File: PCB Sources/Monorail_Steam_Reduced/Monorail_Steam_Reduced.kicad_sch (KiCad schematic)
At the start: 140 parts, among them J6 USB_C_Receptacle_USB2.0, J8 Conn_01x04_Male, J9 Conn_01x03_Male, SW3 RotaryEncoder_Switch, U1 SRV05-4, U2 XC6206PxxxMR, U3 RP2040TR7, U4 W25Q128JVS, Y1 Crystal_GND24_Small

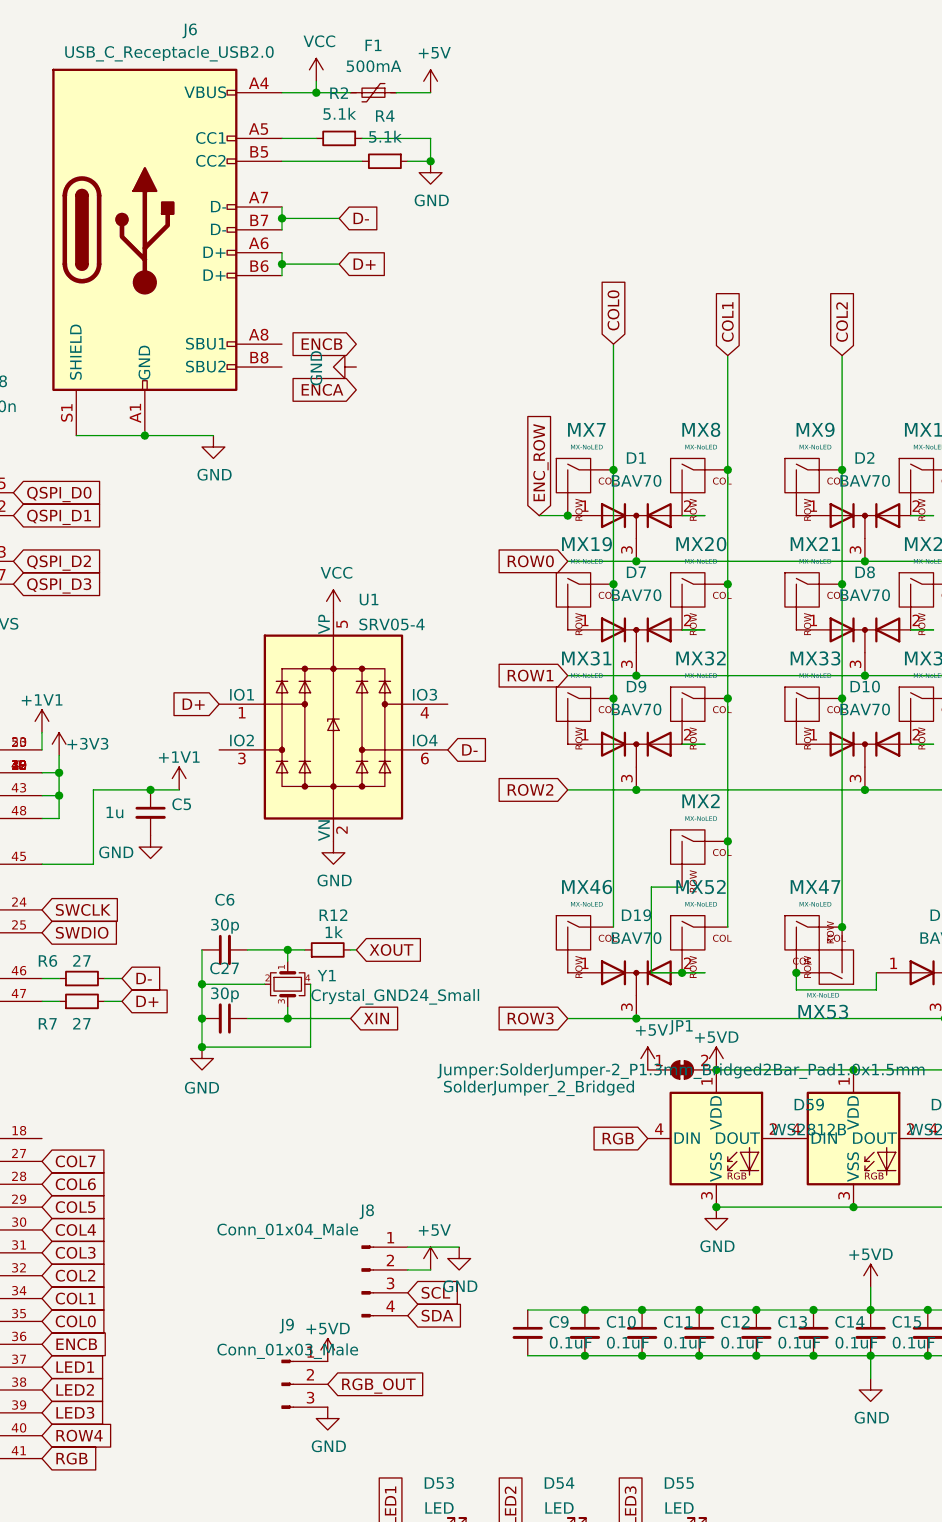
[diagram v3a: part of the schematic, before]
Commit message: set initial positions for components
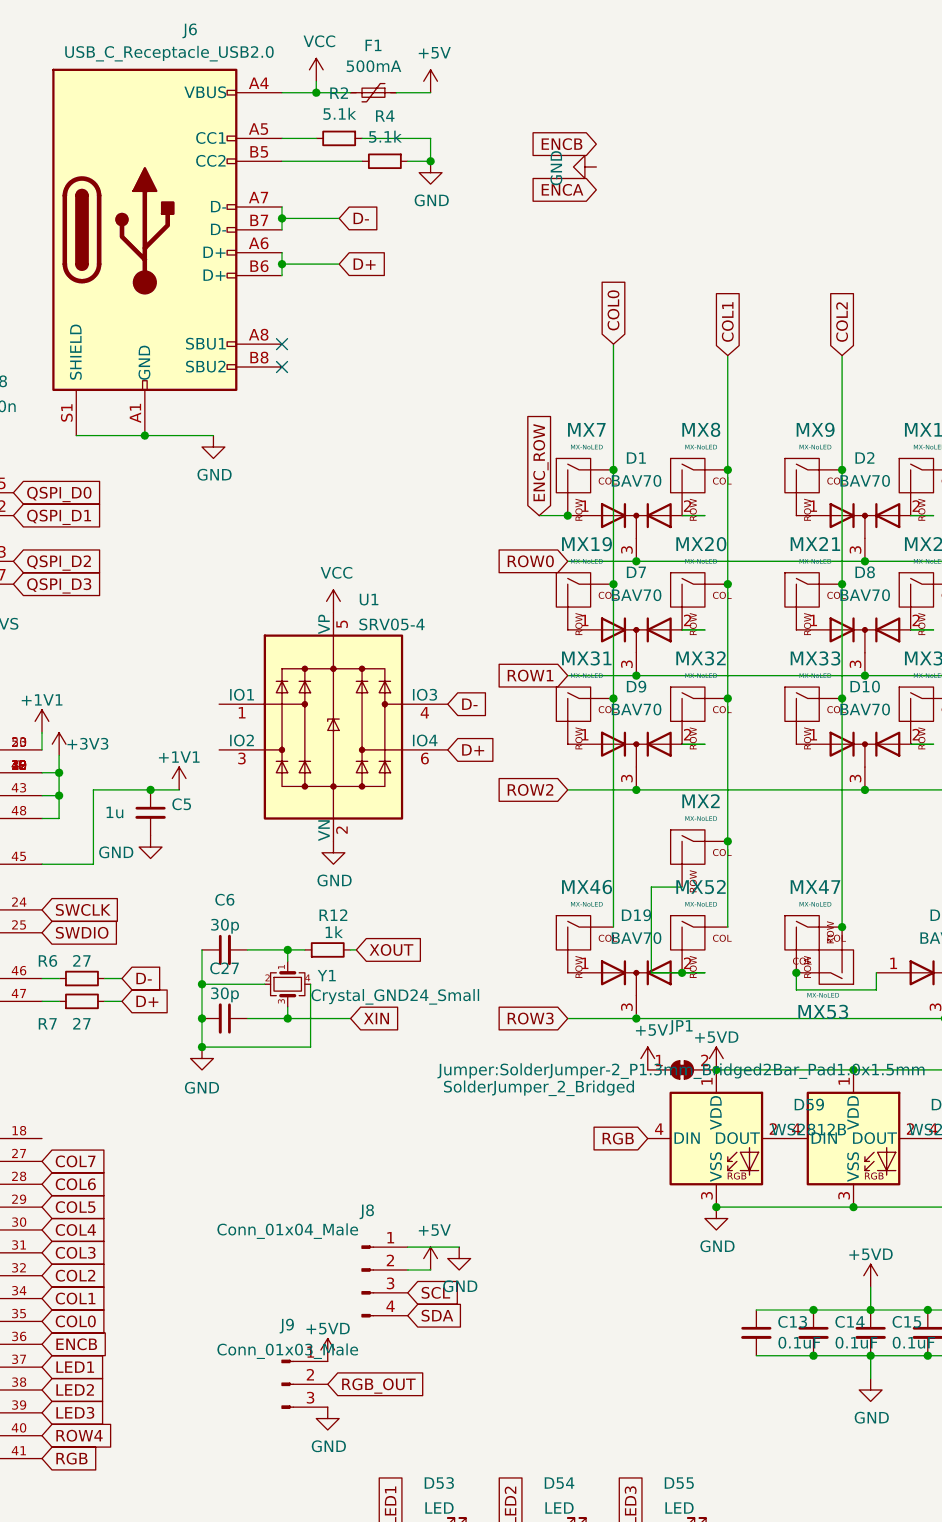
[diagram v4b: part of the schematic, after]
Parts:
- removed C10, C11, C12, C9: 0.1uF, Capacitor_SMD:C_0603_1608Metric, symbol Device:C_Small
- J6: footprint Type-C:HRO-TYPE-C-31-M-12-Assembly -> Connector_USB:USB_C_Receptacle_HRO_TYPE-C-31-M-12
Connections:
- net D+: now also U1.6 (IO4); no longer U1.1 (IO1)
- net D-: now also U1.4 (IO3); no longer U1.6 (IO4)
- no-connect marks 0 -> 2

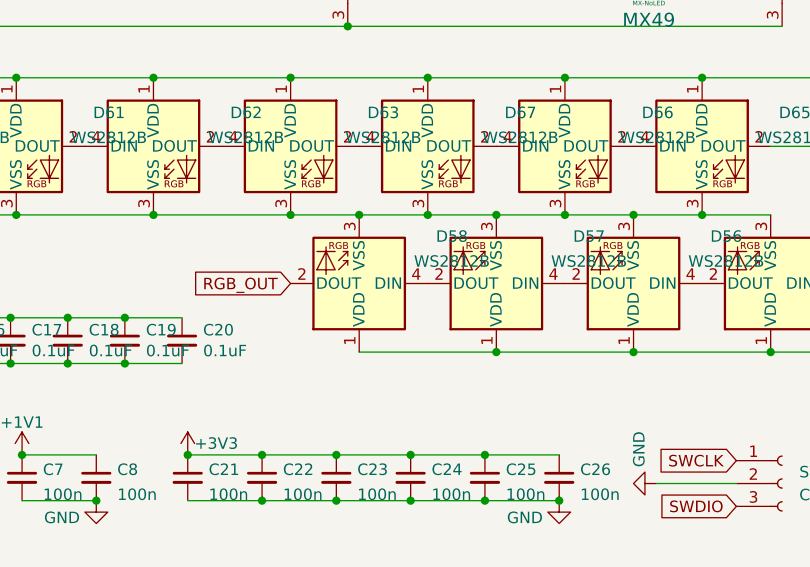
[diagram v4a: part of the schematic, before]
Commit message: began routing upper portion, improved placement
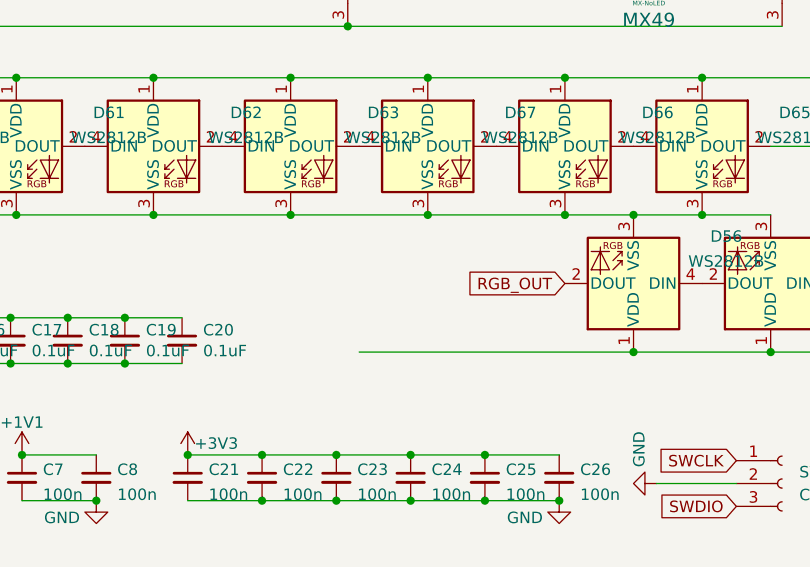
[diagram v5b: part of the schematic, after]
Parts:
- removed D57, D58: WS2812B, WS2812B:WS2812B_data-bridgeable, symbol LED:WS2812B
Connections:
- net RGB_OUT: now also D56.2 (DOUT)
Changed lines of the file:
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@@
   (junction (at 60.325 52.07) (diameter 0) (color 0 0 0 0)
   )
-  (junction (at 219.71 145.415) (diameter 0) (color 0 0 0 0)
-  )
   (junction (at 190.5 88.9) (diameter 0) (color 0 0 0 0)
   )
@@
   (junction (at 193.675 161.925) (diameter 0) (color 0 0 0 0)
   )
-  (junction (at 234.95 145.415) (diameter 0) (color 0 0 0 0)
-  )
   (junction (at 225.425 177.165) (diameter 0) (color 0 0 0 0)
   )
@@
   (junction (at 241.935 177.165) (diameter 0) (color 0 0 0 0)
   )
-  (junction (at 234.95 160.655) (diameter 0) (color 0 0 0 0)
-  )
   (junction (at 265.43 160.655) (diameter 0) (color 0 0 0 0)
   )
@@
     (stroke (width 0) (type default))
   )
-  (wire (pts (xy 219.71 145.415) (xy 227.33 145.415))
+  (wire (pts (xy 212.09 145.415) (xy 227.33 145.415))
     (stroke (width 0) (type default))
   )
@@
     (stroke (width 0) (type default))
   )
-  (wire (pts (xy 234.95 145.415) (xy 242.57 145.415))
+  (wire (pts (xy 227.33 145.415) (xy 242.57 145.415))
     (stroke (width 0) (type default))
   )
@@
     (stroke (width 0) (type default))
   )
-  (wire (pts (xy 219.71 160.655) (xy 234.95 160.655))
+  (wire (pts (xy 219.71 160.655) (xy 250.19 160.655))
     (stroke (width 0) (type default))
   )
@@
     (stroke (width 0) (type default))
   )
-  (wire (pts (xy 212.09 145.415) (xy 219.71 145.415))
-    (stroke (width 0) (type default))
-  )
   (wire (pts (xy 210.82 106.68) (xy 210.82 119.38))
     (stroke (width 0) (type default))
@@
     (stroke (width 0) (type default))
   )
-  (wire (pts (xy 227.33 145.415) (xy 234.95 145.415))
-    (stroke (width 0) (type default))
-  )
   (wire (pts (xy 259.08 119.38) (xy 261.62 119.38))
     (stroke (width 0) (type default))
@@
     (stroke (width 0) (type default))
   )
-  (wire (pts (xy 234.95 160.655) (xy 250.19 160.655))
-    (stroke (width 0) (type default))
-  )
   (wire (pts (xy 203.2 50.8) (xy 203.2 63.5))
     (stroke (width 0) (type default))
@@
     )
   )
-  (global_label "RGB_OUT" (shape input) (at 212.09 153.035 180) (fields_autoplaced)
+  (global_label "RGB_OUT" (shape input) (at 242.57 153.035 180) (fields_autoplaced)
     (effects (font (size 1.27 1.27)) (justify right))
-    (property "Intersheetrefs" "${INTERSHEET_REFS}" (at 201.3596 152.9556 0)
+    (property "Intersheetrefs" "${INTERSHEET_REFS}" (at 231.8396 152.9556 0)
       (effects (font (size 1.27 1.27)) (justify right) hide)
     )
@@
     )
   )
-  (symbol (lib_id "LED:WS2812B") (at 219.71 153.035 180) (unit 1)
-    (in_bom yes) (on_board yes) (dnp no) (fields_autoplaced)
-    (property "Reference" "D58" (at 230.0159 147.811 0)
-      (effects (font (size 1.27 1.27)))
-    )
-    (property "Value" "WS2812B" (at 230.0159 150.5861 0)
-      (effects (font (size 1.27 1.27)))
-    )
-    (property "Footprint" "WS2812B:WS2812B_data-bridgeable" (at 218.44 145.415 0)
-      (effects (font (size 1.27 1.27)) (justify left top) hide)
-    )
-    (property "Datasheet" "https://cdn-shop.adafruit.com/datasheets/WS2812B.pdf" (at 217.17 143.51 0)
-      (effects (font (size 1.27 1.27)) (justify left top) hide)
-    )
-    (pin "1")
-    (pin "2")
-    (pin "3")
-    (pin "4")
-    (instances
-      (project "Monorail_Steam_Reduced"
-        (path "/a3e4f0ae-9f86-49e9-b386-ed8b42e012fb"
-          (reference "D58") (unit 1)
-        )
-      )
-    )
-  )
   (symbol (lib_id "power:GND") (at 252.73 175.26 270) (unit 1)
     (in_bom yes) (on_board yes) (dnp no)
@@
         )
       )
-    )
-  )
-  (symbol (lib_id "LED:WS2812B") (at 234.95 153.035 180) (unit 1)
-    (in_bom yes) (on_board yes) (dnp no) (fields_autoplaced)
-    (property "Reference" "D57" (at 245.2559 147.811 0)
-      (effects (font (size 1.27 1.27)))
-    )
-    (property "Value" "WS2812B" (at 245.2559 150.5861 0)
-      (effects (font (size 1.27 1.27)))
-    )
-    (property "Footprint" "WS2812B:WS2812B_data-bridgeable" (at 233.68 145.415 0)
-      (effects (font (size 1.27 1.27)) (justify left top) hide)
-    )
-    (property "Datasheet" "https://cdn-shop.adafruit.com/datasheets/WS2812B.pdf" (at 232.41 143.51 0)
-      (effects (font (size 1.27 1.27)) (justify left top) hide)
-    )
-    (pin "1")
-    (pin "2")
-    (pin "3")
-    (pin "4")
-    (instances
-      (project "Monorail_Steam_Reduced"
-        (path "/a3e4f0ae-9f86-49e9-b386-ed8b42e012fb"
-          (reference "D57") (unit 1)
-        )
-      )
